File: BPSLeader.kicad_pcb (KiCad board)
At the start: 2 copper layers, 100 x 75 mm, 154 parts, among them J1 GPIO Analyzer, J10 CAN_Out, J11 ErrorLightConn, J12 USB_B_Micro, J13 FanBrdConn, J2 Volt/Temp SPI Analyzer, J3 Current SPI Analyzer, J4 CAN Analyzer, J5 SWD, J6 PowerConn, J7 MinionConn, J8 CurrentConn, J9 ContactorConn, Q1 NTR4003NT1G, Q2 VND5N07-E, Q3 NTR4003NT1G, Q4 VND5N07-E, SW1 B3SL-1002P, U1 STM32F413RHTx, U10 ADM3055E, U11 CDSOT23-T24CAN, U12 SI8261ABC-IS, U13 CP2102N-A01-GQFN24, U14 SI8261ABC-IS, U15 SI8261ABC-IS, U16 SI8261ABC-IS, U17 SI8261ABC-IS, U18 MCP112, U19 RN4871-I, U2 RI3-1205S, U3 NCP1117-3.3_SOT223, U4 M24128, U5 LTC6820, U6 LTC6820, U7 HX1188FNL, U8 SI8261ABC-IS, U9 BAS70-04, Y1 8M

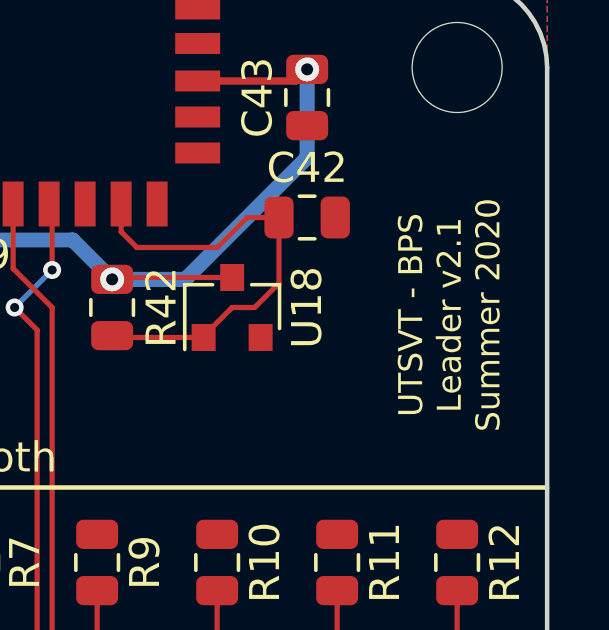
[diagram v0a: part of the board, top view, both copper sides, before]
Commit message: Changes version number to v3.0
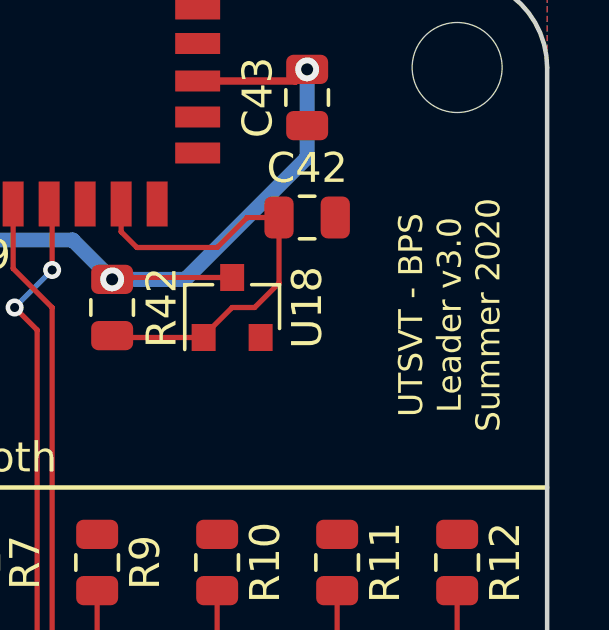
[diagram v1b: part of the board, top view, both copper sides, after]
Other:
- board text added: "UTSVT - BPS Leader v3.0 Summer 2020"
- board text removed: "UTSVT - BPS Leader v2.1 Summer 2020"

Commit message: Moves BAS70-04 to utsvt-chips because other systems use this component
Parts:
- C1, C2: value 10p -> 12p
- D14: value SP0503BAHT -> SP0503BAHTG
- R38, R39, R40, R41: value 117 -> 118
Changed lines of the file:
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@@
       (effects (font (size 1 1) (thickness 0.15)))
     )
-    (fp_text value 10p (at 0 1.65) (layer F.Fab)
+    (fp_text value 12p (at 0 1.65) (layer F.Fab)
       (effects (font (size 1 1) (thickness 0.15)))
     )
@@
       (effects (font (size 1 1) (thickness 0.15)))
     )
-    (fp_text value 10p (at 0 1.65) (layer F.Fab)
+    (fp_text value 12p (at 0 1.65) (layer F.Fab)
       (effects (font (size 1 1) (thickness 0.15)))
     )
@@
       (effects (font (size 1 1) (thickness 0.15)))
     )
-    (fp_text value SP0503BAHT (at -0.28 2.48 90) (layer F.Fab)
+    (fp_text value SP0503BAHTG (at -0.28 2.48 90) (layer F.Fab)
       (effects (font (size 1 1) (thickness 0.15)))
     )
@@
       (effects (font (size 1 1) (thickness 0.15)))
     )
-    (fp_text value 117 (at 0 1.65 90) (layer F.Fab)
+    (fp_text value 118 (at 0 1.65 90) (layer F.Fab)
       (effects (font (size 1 1) (thickness 0.15)))
     )
@@
       (effects (font (size 1 1) (thickness 0.15)) (justify mirror))
     )
-    (fp_text value 117 (at 0 -1.65 90) (layer B.Fab)
+    (fp_text value 118 (at 0 -1.65 90) (layer B.Fab)
       (effects (font (size 1 1) (thickness 0.15)) (justify mirror))
     )
@@
       (effects (font (size 1 1) (thickness 0.15)))
     )
-    (fp_text value 117 (at 0 1.65 90) (layer F.Fab)
+    (fp_text value 118 (at 0 1.65 90) (layer F.Fab)
       (effects (font (size 1 1) (thickness 0.15)))
     )
@@
       (effects (font (size 1 1) (thickness 0.15)) (justify mirror))
     )
-    (fp_text value 117 (at 0 -1.65 90) (layer B.Fab)
+    (fp_text value 118 (at 0 -1.65 90) (layer B.Fab)
       (effects (font (size 1 1) (thickness 0.15)) (justify mirror))
     )

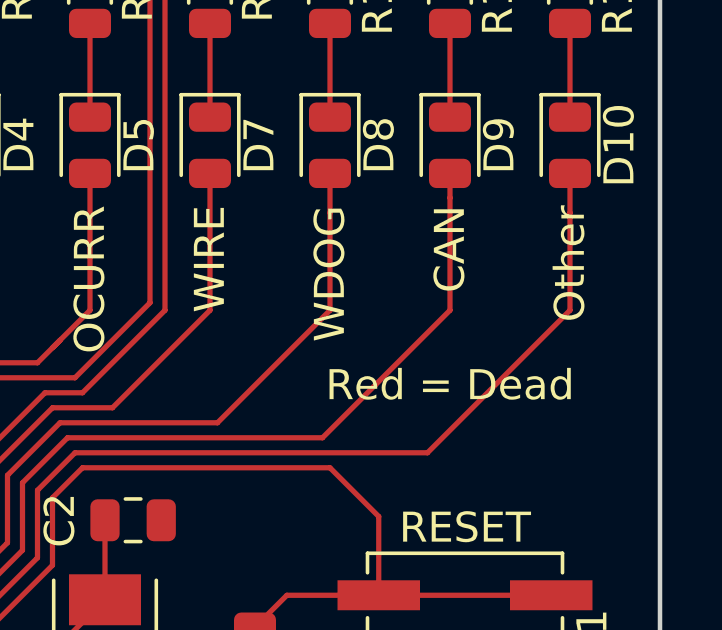
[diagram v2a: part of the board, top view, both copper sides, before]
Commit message: Makes LED silkscreen labels consistent. Changed Other to all caps OTHER
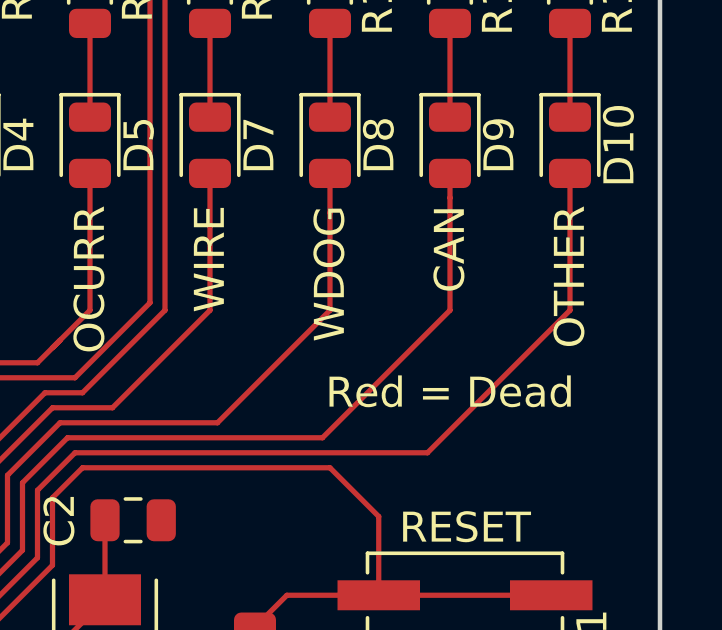
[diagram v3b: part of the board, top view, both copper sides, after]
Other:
- board text added: "OTHER"
- board text removed: "Other"
